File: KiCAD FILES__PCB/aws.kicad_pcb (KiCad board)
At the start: 2 copper layers, 214.9 x 91.5 mm, 33 parts, among them J17 B4B-XH-A_LF__SN_, J20 B3B-XH-A_LF__SN_, J21 B3B-XH-A_LF__SN_, J25 Screw_Terminal_01x02, J26 Screw_Terminal_01x02, J27 Screw_Terminal_01x02, J28 B4B-XH-A_LF__SN_, J3 B3B-XH-A_LF__SN_, J32 B3B-XH-A_LF__SN_, J37 B3B-XH-A_LF__SN_, J39 Conn_01x02_Pin, SW6 SW_SPST

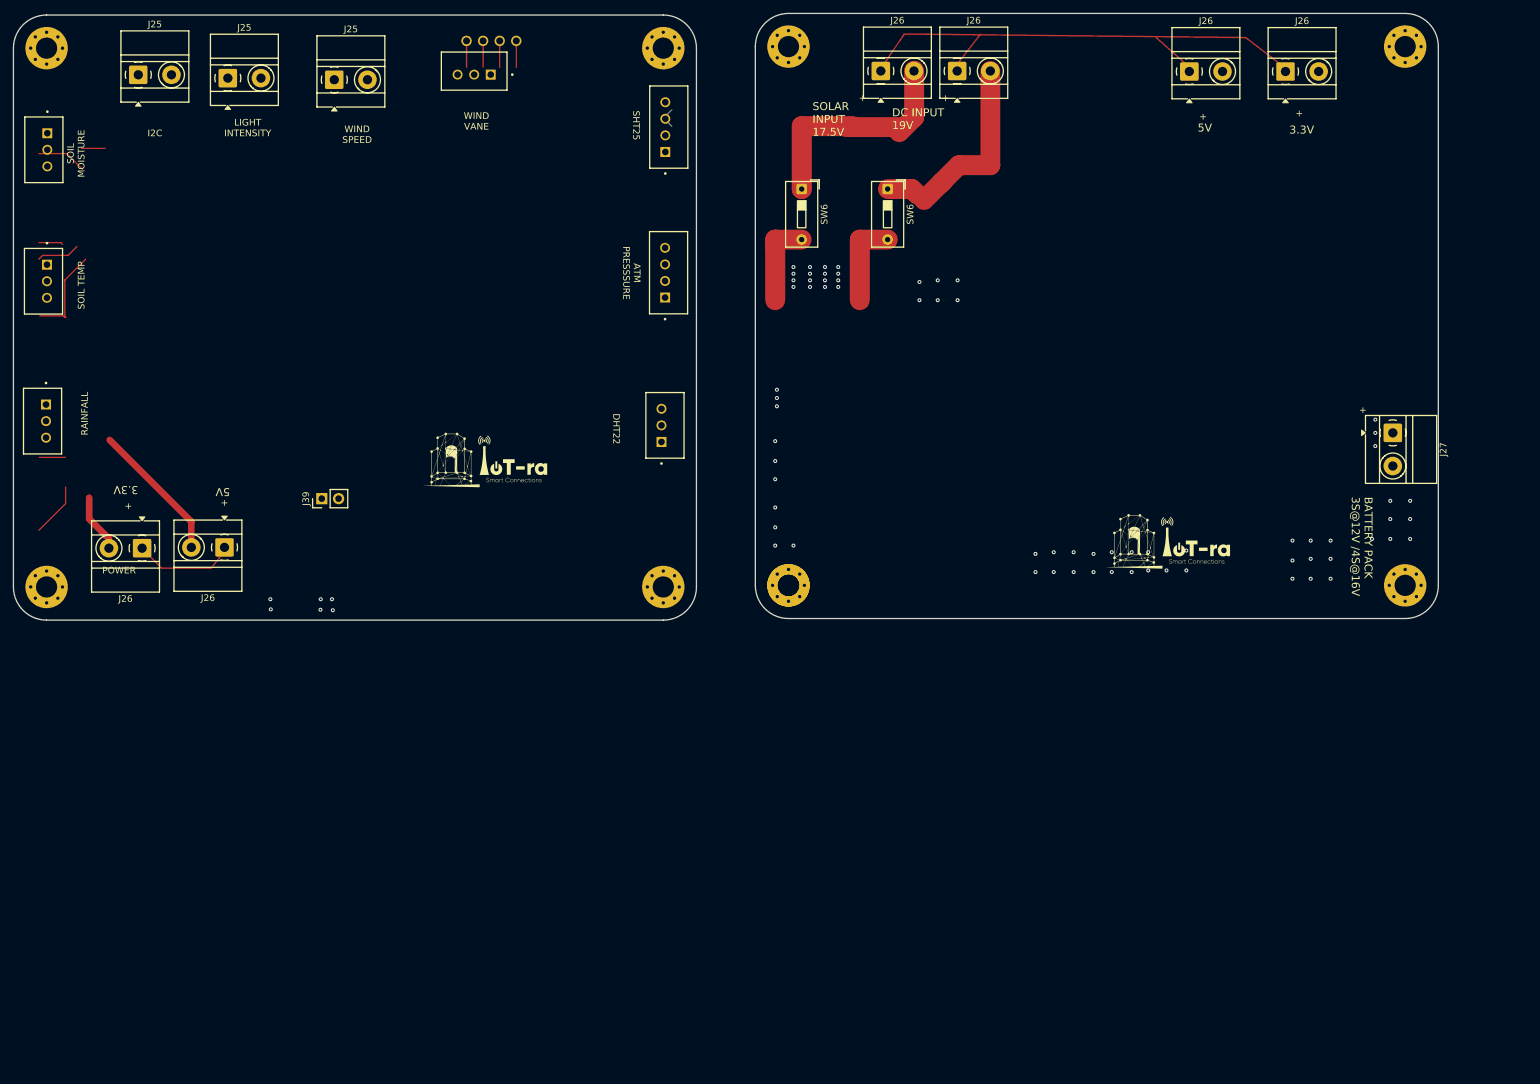
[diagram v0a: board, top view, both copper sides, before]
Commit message: [1st] Updated component placement on pcb design.
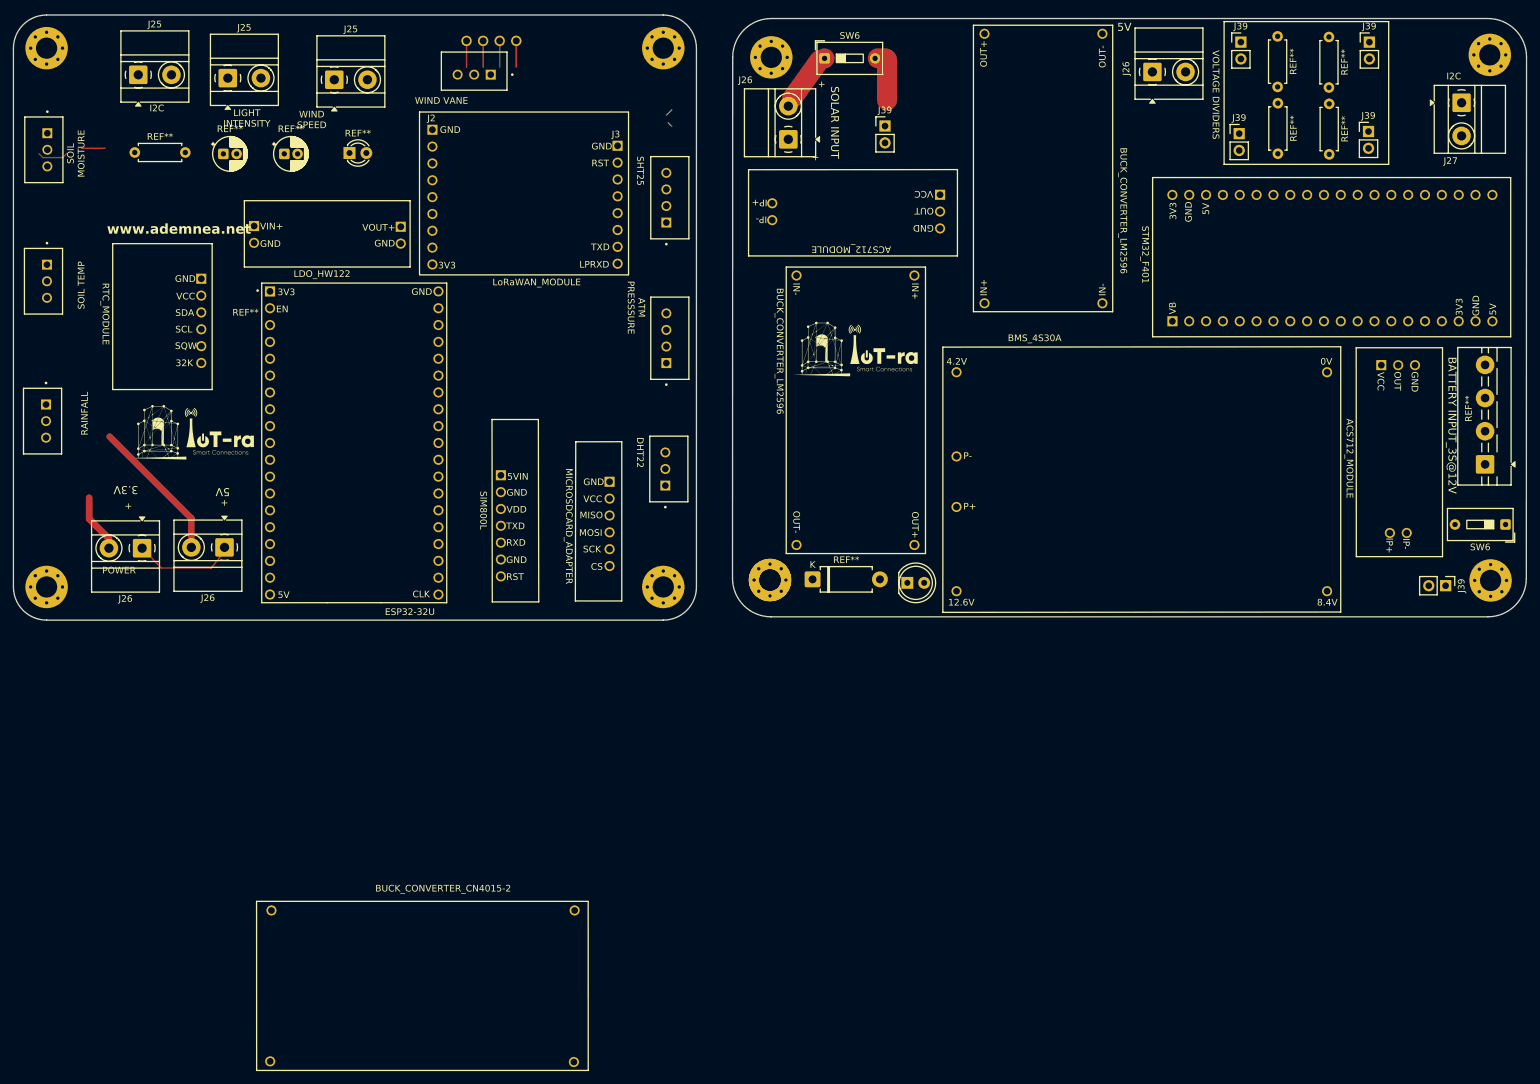
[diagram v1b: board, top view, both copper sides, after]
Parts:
- removed the J26 at (227.5, 45.6)
- removed the J26 at (178.0, 45.5)
- removed the J26 at (213.0, 45.6)
- removed the J39 at (82.2, 110.0)
- added ?: , , F.Cu at (248.5, 83.3)
- added ?: , , F.Cu at (126.8, 59.4)
- added ?: , , F.Cu at (240.9, 64.2)
- added ?: , , F.Cu at (98.8, 69.6)
- added ?: , , F.Cu at (230.8, 64.2)
- added ?: , , F.Cu at (150.1, 68.0)
- added ?: , , F.Cu at (246.0, 64.2)
- added ?: , , F.Cu at (245.8, 115.2)
- added ?: , , F.Cu at (109.2, 111.6)
- added ?: , , F.Cu at (125.6, 120.2)
- added ?: , , F.Cu at (247.0, 89.9)
- added ?: , , F.Cu at (210.4, 83.3)
- added ?: , , F.Cu at (150.1, 65.5)
- added ?: , , F.Cu at (182.1, 39.9)
- added ?: , , F.Cu at (109.2, 109.0)
- added ?: , , F.Cu at (94.1, 71.6)
- added ?: , , F.Cu at (210.4, 64.2)
- added ?: , , F.Cu at (233.8, 124.0)
- added ?: , , F.Cu at (98.8, 62.0)
- added ?: , , F.Cu at (125.6, 115.1)
- added ?: , , F.Cu at (120.3, 172.1)
- added ?: , , F.Cu at (109.2, 121.8)
- added ?: , , F.Cu at (235.8, 64.2)
- added ?: , , F.Cu at (215.5, 83.3)
- added ?: , , F.Cu at (223.1, 64.2)
- added ?: , , F.Cu at (126.8, 56.8)
- added ?: , , F.Cu at (213.0, 83.3)
- added ?: , , F.Cu at (199.9, 80.6)
- added ?: , , F.Cu at (228.2, 83.3)
- added ?: , , F.Cu at (218.1, 64.2)
- added ?: , , F.Cu at (177.9, 91.0)
- added ?: , , F.Cu at (126.8, 67.0)
- added ?: , , F.Cu at (125.6, 110.0)
- added ?: , , F.Cu at (72.0, 68.9)
- added ?: , , F.Cu at (72.0, 71.5)
- added ?: , , F.Cu at (220.6, 64.2)
- added ?: , , F.Cu at (240.9, 83.3)
- added ?: , , F.Cu at (251.1, 64.2)
- added ?: , , F.Cu at (109.2, 106.5)
- added ?: , , F.Cu at (125.6, 112.6)
- added ?: , , F.Cu at (256.2, 64.2)
- added ?: , , F.Cu at (153.8, 117.0)
- added ?: , , F.Cu at (98.8, 74.7)
- added ?: , , F.Cu at (228.2, 64.2)
- added ?: , , F.Cu at (98.8, 59.5)
- added ?: , , F.Cu at (125.6, 107.5)
- added ?: , , F.Cu at (223.1, 83.3)
- added ?: , , F.Cu at (248.5, 64.2)
- added ?: , , F.Cu at (64.0, 87.0)
- added ?: , , F.Cu at (233.8, 91.0)
- added ?: , , F.Cu at (74.4, 194.9)
- added ?: , , F.Cu at (175.4, 69.3)
- added ?: , , F.Cu at (253.6, 64.2)
- added ?: , , F.Cu at (126.8, 64.4)
- added ?: , , F.Cu at (220.6, 83.3)
- added ?: , , F.Cu at (126.8, 72.1)
- added ?: , , F.Cu at (225.7, 64.2)
- added ?: , , F.Cu at (235.8, 83.3)
- added ?: , , F.Cu at (233.3, 83.3)
- added ?: , , F.Cu at (243.2, 115.2)
- added ?: , , F.Cu at (253.6, 83.3)
- added ?: , , F.Cu at (171.5, 117.0)
- added ?: , , F.Cu at (258.7, 64.2)
- added ?: , , F.Cu at (256.2, 83.3)
- added ?: , , F.Cu at (153.8, 76.4)
- added ?: , , F.Cu at (243.5, 64.2)
- added ?: , , F.Cu at (126.8, 69.5)
- added ?: , , F.Cu at (98.8, 56.9)
- added ?: , , F.Cu at (98.8, 54.4)
- added ?: , , F.Cu at (215.5, 64.2)
- added ?: , , F.Cu at (175.4, 66.7)
- added ?: , , F.Cu at (98.8, 67.1)
- added ?: , , F.Cu at (74.6, 172.1)
- added ?: , , F.Cu at (258.7, 83.3)
- added ?: , , F.Cu at (199.9, 39.9)
- added ?: , , F.Cu at (109.2, 116.7)
- added ?: , , F.Cu at (64.0, 76.9)
- added ?: , , F.Cu at (182.1, 80.6)
- added ?: , , F.Cu at (109.2, 114.1)
- added ?: , , F.Cu at (171.5, 76.4)
- added ?: , , F.Cu at (238.4, 83.3)
- added ?: , , F.Cu at (244.5, 89.9)
- added ?: , , F.Cu at (177.9, 124.0)
- added ?: , , F.Cu at (243.5, 83.3)
- added ?: , , F.Cu at (241.9, 89.9)
- added ?: , , F.Cu at (64.0, 89.6)
- added ?: , , F.Cu at (120.2, 195.0)
- added ?: , , F.Cu at (64.0, 84.5)
- added ?: , , F.Cu at (109.2, 119.2)
- added ?: , , F.Cu at (177.9, 103.7)
- added ?: , , F.Cu at (126.8, 74.6)
- added ?: , , F.Cu at (175.4, 64.2)
- added ?: , , F.Cu at (126.8, 61.9)
- added ?: , , F.Cu at (218.1, 83.3)
- added ?: , , F.Cu at (64.0, 82.0)
- added ?: , , F.Cu at (238.4, 64.2)
- added ?: , , F.Cu at (213.0, 64.2)
- added ?: , , F.Cu at (94.1, 69.0)
- added ?: , , F.Cu at (230.8, 83.3)
- added ?: , , F.Cu at (246.0, 83.3)
- added ?: , , F.Cu at (233.3, 64.2)
- added ?: , , F.Cu at (98.8, 64.6)
- added ?: , , F.Cu at (177.9, 111.3)
- added ?: , , F.Cu at (225.7, 83.3)
- added ?: , , F.Cu at (251.1, 83.3)
- added ?: , , F.Cu at (125.6, 117.7)
- added ?: , , F.Cu at (64.0, 79.4)
- added ?: , , F.Cu at (98.8, 72.2)
- added J26: Screw_Terminal_01x02, TerminalBlock_MetzConnect:TerminalBlock_MetzConnect_Type011_RT05502HBWC_1x02_P5.00mm_Horizontal, F.Cu at (207.4, 45.7)
- added J39: Conn_01x02_Pin, Connector_PinHeader_2.54mm:PinHeader_1x02_P2.54mm_Vertical, F.Cu at (220.5, 55.0)
- added J39: Conn_01x02_Pin, Connector_PinHeader_2.54mm:PinHeader_1x02_P2.54mm_Vertical, F.Cu at (220.8, 41.2)
- added J39: Conn_01x02_Pin, Connector_PinHeader_2.54mm:PinHeader_1x02_P2.54mm_Vertical, F.Cu at (240.2, 41.2)
- added J39: Conn_01x02_Pin, Connector_PinHeader_2.54mm:PinHeader_1x02_P2.54mm_Vertical, F.Cu at (251.6, 123.2)
- added J39: Conn_01x02_Pin, Connector_PinHeader_2.54mm:PinHeader_1x02_P2.54mm_Vertical, F.Cu at (167.1, 53.8)
- added J39: Conn_01x02_Pin, Connector_PinHeader_2.54mm:PinHeader_1x02_P2.54mm_Vertical, F.Cu at (240.0, 54.7)
- added REF**: R_Axial_DIN0207_L6.3mm_D2.5mm_P7.62mm_Horizontal, Resistor_THT:R_Axial_DIN0207_L6.3mm_D2.5mm_P7.62mm_Horizontal, F.Cu at (54.0, 57.8)
- added REF**: R_Axial_DIN0207_L6.3mm_D2.5mm_P7.62mm_Horizontal, Resistor_THT:R_Axial_DIN0207_L6.3mm_D2.5mm_P7.62mm_Horizontal, F.Cu at (226.3, 40.3)
- added REF**: MODULE_ESP32-DEVKITC-32U, MODULE_ESP32-DEVKITC-32U:MODULE_ESP32-DEVKITC-32U, F.Cu at (87.1, 101.6)
- added REF**: LED_D3.0mm, LED_THT:LED_D3.0mm, F.Cu at (86.3, 57.9)
- added REF**: D_DO-15_P10.16mm_Horizontal, Diode_THT:D_DO-15_P10.16mm_Horizontal, F.Cu at (156.2, 122.2)
- added REF**: TerminalBlock_MaiXu_MX126-5.0-04P_1x04_P5.00mm, TerminalBlock:TerminalBlock_MaiXu_MX126-5.0-04P_1x04_P5.00mm, F.Cu at (257.6, 104.9)
- added REF**: R_Axial_DIN0207_L6.3mm_D2.5mm_P7.62mm_Horizontal, Resistor_THT:R_Axial_DIN0207_L6.3mm_D2.5mm_P7.62mm_Horizontal, F.Cu at (234.1, 40.4)
- added REF**: CP_Radial_D5.0mm_P2.00mm, Capacitor_THT:CP_Radial_D5.0mm_P2.00mm, F.Cu at (76.5, 58.0)
- added REF**: R_Axial_DIN0207_L6.3mm_D2.5mm_P7.62mm_Horizontal, Resistor_THT:R_Axial_DIN0207_L6.3mm_D2.5mm_P7.62mm_Horizontal, F.Cu at (234.1, 50.5)
- added REF**: R_Axial_DIN0207_L6.3mm_D2.5mm_P7.62mm_Horizontal, Resistor_THT:R_Axial_DIN0207_L6.3mm_D2.5mm_P7.62mm_Horizontal, F.Cu at (226.3, 50.4)
- added REF**: LED_D5.0mm, LED_THT:LED_D5.0mm, F.Cu at (170.5, 122.7)
- added REF**: CP_Radial_D5.0mm_P2.00mm, Capacitor_THT:CP_Radial_D5.0mm_P2.00mm, F.Cu at (67.3, 58.0)
- moved SW6 106.0 mm to (260.7, 113.9), turned to 180 degrees
- moved J27 50.8 mm to (254.1, 50.3)
- moved SW6 20.0 mm to (158.0, 43.6), turned to 0 degrees
- moved J26 17.3 mm to (152.5, 55.8), turned to 90 degrees
- moved REF** 12.9 mm to (258.4, 122.4)
- moved REF** 12.8 mm to (258.3, 43.1)
- moved J17 10.7 mm to (134.7, 64.7)
- moved J28 9.88 mm to (134.7, 85.8)
- moved J32 6.61 mm to (134.5, 105.6)
- moved REF** 3.06 mm to (150.0, 43.5)
- moved ? 2.90 mm to (149.8, 122.3)
- moved REF** 2.90 mm to (149.8, 122.3)
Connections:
- J26 pad 1: GND -> (no net)
- J26 pad 2: Net-(J26-Pin_2) -> (no net) (x2)
- J27 pad 1: /power board/BATTERY BMS -> (no net)
- J27 pad 2: GND -> (no net)
- SW6 pad 1: Net-(J25-Pin_2) -> (no net) (x2)
- SW6 pad 2: /power board/SOLAR INPUT -> (no net) (x2)
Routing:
- net Net-(J26-Pin_2): track 66.7 -> 29.8 mm
- net Net-(J25-Pin_2): track 29.8 -> 0.00 mm
- net /power board/SOLAR INPUT: track 27.2 -> 1.15 mm
- net /gate way/DAVIS 7852: track 14.3 -> 0.00 mm
- net /gate way/DHT22: track 12.1 -> 0.00 mm
- net GND: track 6.56 -> 0.00 mm, vias 72 -> 0
- net /gate way/DS18B20: track 3.71 -> 0.00 mm
- net /gate way/VH400: track 11.1 -> 8.24 mm
- net /power board/BATTERY BMS: vias 3 -> 0
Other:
- board size 214.9 x 91.5 mm -> 228.2 x 91.2 mm
- board text added: "0V"
- board text added: "12.6V"
- board text added: "32K"
- board text added: "3V3"
- board text added: "4.2V"
- board text added: "5VIN"
- board text added: "8.4V"
- board text added: "ACS712_MODULE"
- board text added: "BATTERY INPUT_3S@12V"
- board text added: "BMS_4S30A"
- board text added: "BUCK_CONVERTER_CN4015-2"
- board text added: "BUCK_CONVERTER_LM2596"
- board text added: "CLK"
- board text added: "CS"
- board text added: "EN"
- board text added: "ESP32-32U"
- board text added: "GND"
- board text added: "IN+"
- board text added: "IN-"
- board text added: "IP+"
- board text added: "IP-"
- board text added: "J2"
- board text added: "J3"
- board text added: "LDO_HW122"
- board text added: "LPRXD"
- board text added: "LoRaWAN_MODULE"
- board text added: "MICROSDCARD_ADAPTER"
- board text added: "MISO"
- board text added: "MOSI"
- board text added: "OUT"
- board text added: "OUT+"
- board text added: "OUT-"
- board text added: "P+"
- board text added: "P-"
- board text added: "RST"
- board text added: "RTC_MODULE"
- board text added: "RXD"
- board text added: "SCK"
- board text added: "SCL"
- board text added: "SDA"
- board text added: "SIM800L"
- board text added: "SOLAR INPUT"
- board text added: "SQW"
- board text added: "STM32_F401"
- board text added: "TXD"
- board text added: "VB"
- board text added: "VCC"
- board text added: "VDD"
- board text added: "VIN+"
- board text added: "VOLTAGE DIVIDERS"
- board text added: "VOUT+"
- board text removed: "BATTERY PACK 3S@12V /4S@16V"
- board text removed: "DC INPUT 19V"
- board text removed: "SOLAR INPUT 17.5V"

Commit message: [2nd] Updated Component placement on pcb design.
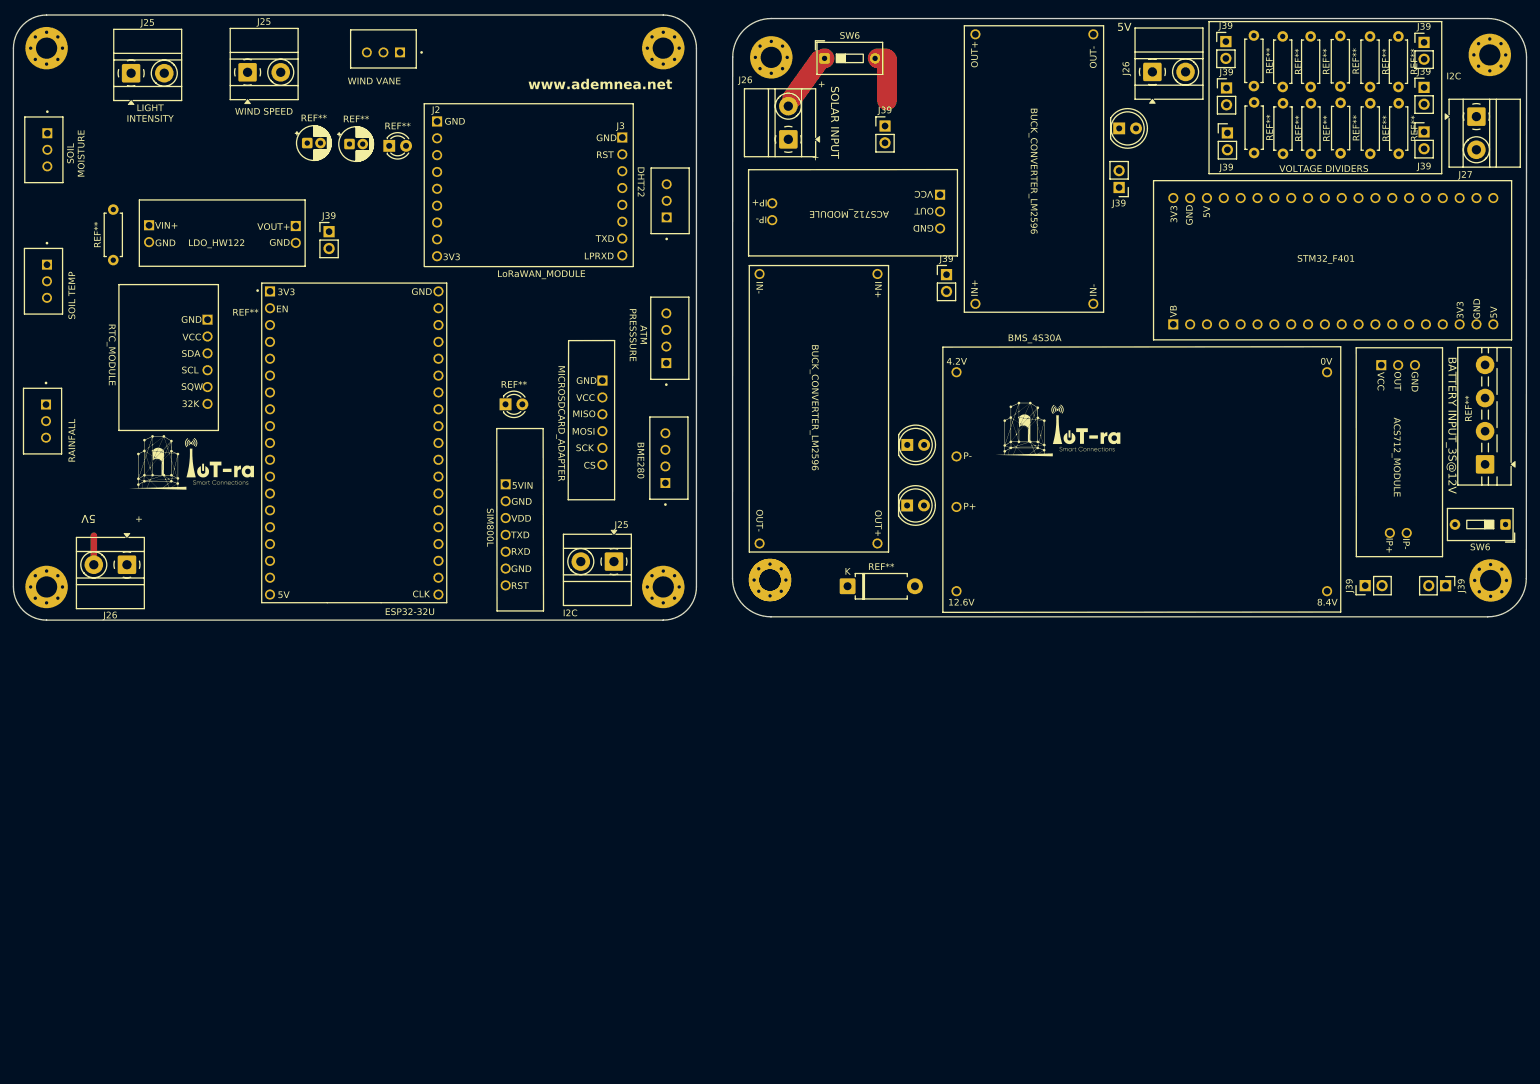
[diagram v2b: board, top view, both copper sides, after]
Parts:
- removed the ? at (104.0, 41.0)
- removed the ? at (120.3, 172.1)
- removed the ? at (74.4, 194.9)
- removed the ? at (109.0, 41.0)
- removed the ? at (106.5, 41.0)
- removed the ? at (74.6, 172.1)
- removed the ? at (120.2, 195.0)
- removed the ? at (111.5, 41.0)
- removed the J26 at (55.1, 117.5)
- added J39: Conn_01x02_Pin, Connector_PinHeader_2.54mm:PinHeader_1x02_P2.54mm_Vertical, F.Cu at (202.4, 63.1)
- added J39: Conn_01x02_Pin, Connector_PinHeader_2.54mm:PinHeader_1x02_P2.54mm_Vertical, F.Cu at (239.5, 123.2)
- added J39: Conn_01x02_Pin, Connector_PinHeader_2.54mm:PinHeader_1x02_P2.54mm_Vertical, F.Cu at (248.4, 48.0)
- added J39: Conn_01x02_Pin, Connector_PinHeader_2.54mm:PinHeader_1x02_P2.54mm_Vertical, F.Cu at (83.3, 69.8)
- added J39: Conn_01x02_Pin, Connector_PinHeader_2.54mm:PinHeader_1x02_P2.54mm_Vertical, F.Cu at (218.6, 48.1)
- added J39: Conn_01x02_Pin, Connector_PinHeader_2.54mm:PinHeader_1x02_P2.54mm_Vertical, F.Cu at (176.4, 76.2)
- added REF**: LED_D5.0mm, LED_THT:LED_D5.0mm, F.Cu at (202.4, 54.2)
- added REF**: R_Axial_DIN0207_L6.3mm_D2.5mm_P7.62mm_Horizontal, Resistor_THT:R_Axial_DIN0207_L6.3mm_D2.5mm_P7.62mm_Horizontal, F.Cu at (240.2, 40.3)
- added REF**: R_Axial_DIN0207_L6.3mm_D2.5mm_P7.62mm_Horizontal, Resistor_THT:R_Axial_DIN0207_L6.3mm_D2.5mm_P7.62mm_Horizontal, F.Cu at (231.3, 40.3)
- added REF**: R_Axial_DIN0207_L6.3mm_D2.5mm_P7.62mm_Horizontal, Resistor_THT:R_Axial_DIN0207_L6.3mm_D2.5mm_P7.62mm_Horizontal, F.Cu at (240.3, 50.4)
- added REF**: R_Axial_DIN0207_L6.3mm_D2.5mm_P7.62mm_Horizontal, Resistor_THT:R_Axial_DIN0207_L6.3mm_D2.5mm_P7.62mm_Horizontal, F.Cu at (235.8, 40.3)
- added REF**: LED_D5.0mm, LED_THT:LED_D5.0mm, F.Cu at (170.5, 101.9)
- added REF**: R_Axial_DIN0207_L6.3mm_D2.5mm_P7.62mm_Horizontal, Resistor_THT:R_Axial_DIN0207_L6.3mm_D2.5mm_P7.62mm_Horizontal, F.Cu at (244.6, 50.4)
- added REF**: R_Axial_DIN0207_L6.3mm_D2.5mm_P7.62mm_Horizontal, Resistor_THT:R_Axial_DIN0207_L6.3mm_D2.5mm_P7.62mm_Horizontal, F.Cu at (231.3, 50.4)
- added REF**: R_Axial_DIN0207_L6.3mm_D2.5mm_P7.62mm_Horizontal, Resistor_THT:R_Axial_DIN0207_L6.3mm_D2.5mm_P7.62mm_Horizontal, F.Cu at (235.8, 50.3)
- added REF**: R_Axial_DIN0207_L6.3mm_D2.5mm_P7.62mm_Horizontal, Resistor_THT:R_Axial_DIN0207_L6.3mm_D2.5mm_P7.62mm_Horizontal, F.Cu at (244.5, 40.3)
- added REF**: LED_D3.0mm, LED_THT:LED_D3.0mm, F.Cu at (109.9, 95.8)
- moved J25 102.6 mm to (126.2, 119.5), turned to 180 degrees
- moved J32 40.4 mm to (134.7, 65.1)
- moved J17 39.3 mm to (134.5, 103.9)
- moved REF** 16.6 mm to (50.7, 74.1), turned to 90 degrees
- moved ? 15.8 mm to (78.2, 71.5)
- moved ? 15.8 mm to (78.2, 68.9)
- moved ? 15.8 mm to (56.1, 68.8)
- moved ? 15.8 mm to (56.1, 71.3)
- moved ? 15.3 mm to (124.5, 99.8)
- moved ? 15.3 mm to (124.5, 94.8)
- moved ? 15.3 mm to (124.5, 102.4)
- moved ? 15.3 mm to (124.5, 104.9)
- moved ? 15.3 mm to (124.5, 97.3)
- moved ? 15.3 mm to (124.5, 92.2)
- moved J26 14.9 mm to (52.8, 120.0)
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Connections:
- J17 pad 1: +3.3V_LORA -> (no net)
- J17 pad 2: /gate way/I2C SCL -> (no net)
- J17 pad 3: /gate way/I2C SDA -> (no net)
- J17 pad 4: GND -> (no net)
- J20 pad 1: 5v -> (no net)
- J20 pad 2: /gate way/VH400 -> (no net)
- J20 pad 3: GND -> (no net)
- J21 pad 1: 5v -> (no net)
- J21 pad 3: GND -> (no net)
- J25 pad 1: GND -> (no net) (x3)
- J25 pad 2: Net-(J25-Pin_2) -> (no net) (x2)
- J26 pad 1: GND -> (no net)
- J28 pad 4: GND -> (no net)
- J3 pad 1: /gate way/DAVIS 7852 -> (no net)
- J3 pad 2: GND -> (no net)
- J3 pad 3: GND -> (no net)
- J37 pad 1: 5v -> (no net)
- J37 pad 3: GND -> (no net)
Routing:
- net Net-(J26-Pin_2): track 29.8 -> 0.01 mm
- net Net-(U8-B): track 15.9 -> 0.00 mm
- net /gate way/VH400: track 8.24 -> 0.00 mm
- net (no net): track 0.00 -> 3.50 mm
- net /gate way/I2C SDA: track 1.92 -> 0.00 mm
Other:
- board text added: "BME280"
- board text removed: "3.3V"
- board text removed: "3V"
- board text removed: "BUCK_CONVERTER_CN4015-2"
- board text removed: "G"
- board text removed: "POWER"
- board text removed: "SHT25"
